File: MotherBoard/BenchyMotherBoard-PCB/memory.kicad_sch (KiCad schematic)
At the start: 2 parts

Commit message: Add MORE regulators, USB, Display, and SDCard
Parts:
- removed U?: AS4C64M16D3B, Daxxn_Packages:BGA96_9.0x13.0mm_P0.8mm, symbol Daxxn_IC:AS4C64M16D3B
- added C? (x2): 22uF, Capacitor_SMD:C_1210_3225Metric, symbol Device:C_Small
- added C? (x27): 100nF, Capacitor_SMD:C_0603_1608Metric, symbol Device:C_Small
- added R? (x24): 56, Resistor_SMD:R_0402_1005Metric, symbol Device:R_Small_US
- added R? (x2): 10K, Resistor_SMD:R_0402_1005Metric, symbol Device:R_Small_US
- added R? (x2): 240 1%, Resistor_SMD:R_0402_1005Metric, symbol Device:R_Small_US
- added R?: 100, Resistor_SMD:R_0402_1005Metric, symbol Device:R_Small_US
- added U?: IS43TR16256B-125KBLI, Package_BGA:BGA-96_9.0x13.0mm_Layout2x3x16_P0.8mm, symbol Daxxn_IC:IS43TR16256B-125KBLI
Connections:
- net GND: now also C?.2, C?.2, C?.2, C?.2, C?.2, C?.2, C?.2, C?.2, C?.2, C?.2, C?.2, C?.2, C?.2, C?.2, C?.2, C?.2, C?.2, C?.2, C?.2, C?.2, C?.2, C?.2, C?.2, C?.2, C?.2, C?.2, C?.2, C?.2, C?.2, R?.1, R?.1, R?.2, R?.2, U?.A9 (GND), U?.B1 (GNDQ), U?.B3 (GND), U?.B9 (GNDQ), U?.D1 (GNDQ), U?.D8 (GNDQ), U?.E1 (GND), U?.E2 (GNDQ), U?.E8 (GNDQ), U?.F9 (GNDQ), U?.G1 (GNDQ), U?.G8 (GND), U?.G9 (GNDQ), U?.J2 (GND), U?.J8 (GND), U?.M1 (GND), U?.M9 (GND), U?.N1 (GND), U?.P1 (GND), U?.P9 (GND), U?.T1 (GND), U?.T9 (GND)
- net VDD: now also C?.1, C?.1, C?.1, C?.1, C?.1, C?.1, C?.1, C?.1, C?.1, C?.1, C?.1, C?.1, U?.A1 (VDDQ), U?.A8 (VDDQ), U?.B2 (VDD), U?.C1 (VDDQ), U?.C9 (VDDQ), U?.D2 (VDDQ), U?.D9 (VDD), U?.E9 (VDDQ), U?.F1 (VDDQ), U?.G7 (VDD), U?.H2 (VDDQ), U?.H9 (VDDQ), U?.K2 (VDD), U?.K8 (VDD), U?.N9 (VDD), U?.R1 (VDD), U?.R9 (VDD)
- net DDR-DQ0: now reaches U?.A17 (DDR-DQ0)
- net DDR-DQ0: now also U?.D7 (DQU0)
- net DDR-DQ1: now reaches U?.A18 (DDR-DQ1)
- net DDR-DQ1: now also U?.C3 (DQU1)
- net DDR-DQ3: now reaches U?.B17 (DDR-DQ3)
- net DDR-DQ3: now also U?.C2 (DQU3)
- net DDR-DQ7: now reaches U?.B18 (DDR-DQ7)
- net DDR-DQ7: now also U?.A3 (DQU7)
- net DDR-DQSL-: now reaches U?.B19 (DDR-DQS0N)
- net DDR-DQSL-: now also U?.G3 (DQSL-)
- net DDR-DQML: now reaches U?.C18 (DDR-DQM0)
- net DDR-DQML: now also U?.E7 (DML)
- net DDR-DQSL+: now reaches U?.C19 (DDR-DQS0P)
- net DDR-DQSL+: now also U?.F3 (DQSL+)
- net DDR-DQ5: now reaches U?.D17 (DDR-DQ5)
- net DDR-DQ5: now also U?.A2 (DQU5)
- net DDR-DQ2: now reaches U?.D18 (DDR-DQ2)
- net DDR-DQ2: now also U?.C8 (DQU2)
- net DDR-DQ6: now reaches U?.D19 (DDR-DQ6)
- net DDR-DQ6: now also U?.B8 (DQU6)
- net DDR-A7: now reaches U?.E17 (DDR-A7)
- net DDR-A7: now also R?.1, U?.R2 (A7)
- net DDR-DQ4: now reaches U?.E18 (DDR-DQ4)
- net DDR-DQ4: now also U?.A7 (DQU4)
- net DDR-A13: now reaches U?.F17 (DDR-A13)
- net DDR-A13: now also R?.1, U?.T3 (A13)
- net at U?.F18 (DDR-ZQ): now also R?.1
- net DDR-A3: now reaches U?.F19 (DDR-A3)
- net DDR-A3: now also R?.1, U?.N2 (A3)
- net DDR-RESET: now reaches U?.G16 (DDR-RESET)
- net DDR-RESET: now also R?.2, U?.T2 (~{RESET})
- net DDR-A9: now reaches U?.G17 (DDR-A9)
- net DDR-A9: now also R?.1, U?.R3 (A9)
- net DDR-A2: now reaches U?.G18 (DDR-A2)
- net DDR-A2: now also R?.1, U?.P3 (A2)
- net DDR-BA0: now reaches U?.G19 (DDR-BA0)
- net DDR-BA0: now also R?.1, U?.M2 (BA0)
- net DDR-A5: now reaches U?.H17 (DDR-A5)
- net DDR-A5: now also R?.1, U?.P2 (A5)
- net DDR-A0: now reaches U?.H18 (DDR-A0)
- net DDR-A0: now also R?.1, U?.N3 (A0)
- net DDR-ODT: now reaches U?.H19 (DDR-ODT)
- net DDR-ODT: now also R?.1, U?.K1 (ODT)
- net DDR-BA2: now reaches U?.J16 (DDR-BA2)
- net DDR-BA2: now also R?.1, U?.M3 (BA2)
- net DDR-~{WE}: now reaches U?.J17 (DDR-WEN)
- net DDR-~{WE}: now also R?.1, U?.L3 (~{WE})
- net DDR-~{CS}: now reaches U?.J18 (DDR-CSN)
- net DDR-~{CS}: now also R?.1, U?.L2 (~{CS})
- net DDR-~{CAS}: now reaches U?.K17 (DDR-CASN)
- net DDR-~{CAS}: now also R?.1, U?.K3 (~{CAS})
- net DDR-CLK-: now reaches U?.K19 (DDR-CLKN)
- net DDR-CLK-: now also R?.1, U?.K7 (CK-)
- net DDR-A12: now reaches U?.L17 (DDR-A12)
- net DDR-A12: now also R?.1, U?.N7 (A12/~{BC})
- net DDR-~{RAS}: now reaches U?.L18 (DDR-RASN)
- net DDR-~{RAS}: now also R?.1, U?.J3 (~{RAS})
- net DDR-CLK+: now reaches U?.L19 (DDR-CLKP)
- net DDR-CLK+: now also R?.2, U?.J7 (CK+)
- net DDR-A1: now reaches U?.M17 (DDR-A1)
- net DDR-A1: now also R?.1, U?.P7 (A1)
- net DDR-A11: now reaches U?.M18 (DDR-A11)
- net DDR-A11: now also R?.1, U?.R7 (A11)
- net DDR-A10: now reaches U?.M19 (DDR-A10)
- net DDR-A10: now also R?.1, U?.L7 (A10/AP)
- net DDR-A6: now reaches U?.N16 (DDR-A6)
- net DDR-A6: now also R?.1, U?.R8 (A6)
- net DDR-BA1: now reaches U?.N17 (DDR-BA1)
- net DDR-BA1: now also R?.1, U?.N8 (BA1)
- net DDR-A14: now reaches U?.N18 (DDR-A14)
- net DDR-A14: now also R?.1, U?.T7 (A14)
- net DDR-A4: now reaches U?.P17 (DDR-A4)
- net DDR-A4: now also R?.1, U?.P8 (A4)
- net DDR-DQ8: now reaches U?.P18 (DDR-DQ8)
- net DDR-DQ8: now also U?.E3 (DQL0)
- net DDR-CKE: now reaches U?.P19 (DDR-CKE)
- net DDR-CKE: now also R?.1, R?.2, U?.K9 (CKE)
- net DDR-A8: now reaches U?.R17 (DDR-A8)
- net DDR-A8: now also R?.1, U?.T8 (A8)
- net DDR-DQ10: now reaches U?.R18 (DDR-DQ10)
- net DDR-DQ10: now also U?.F2 (DQL2)
- net DDR-DQ9: now reaches U?.T17 (DDR-DQ9)
- net DDR-DQ9: now also U?.F7 (DQL1)
- net DDR-DQ13: now reaches U?.T18 (DDR-DQ13)
- net DDR-DQ13: now also U?.H8 (DQL5)
- net DDR-DQSU-: now reaches U?.T19 (DDR-DQS1N)
- net DDR-DQSU-: now also U?.B7 (DQSU-)
- net DDR-DQMU: now reaches U?.U18 (DDR-DQM1)
- net DDR-DQMU: now also U?.D3 (DMU)
- net DDR-DQSU+: now reaches U?.U19 (DDR-DQS1P)
- net DDR-DQSU+: now also U?.C7 (DQSU+)
- net DDR-DQ14: now reaches U?.V18 (DDR-DQ14)
- net DDR-DQ14: now also U?.G2 (DQL6)
- net DDR-DQ11: now reaches U?.V19 (DDR-DQ11)
- net DDR-DQ11: now also U?.F8 (DQL3)
- net VREF-DDR: now reaches U?.W16 (DDR-VREF)
- net VREF-DDR: now also C?.1, C?.1, C?.1, U?.H1 (VREFQ), U?.M8 (VREFCA)
- net DDR-DQ15: now reaches U?.W17 (DDR-DQ15)
- net DDR-DQ15: now also U?.H7 (DQL7)
- net DDR-DQ12: now reaches U?.W18 (DDR-DQ12)
- net DDR-DQ12: now also U?.H3 (DQL4)
- new net: U?.J1 (NC), U?.J9 (NC), U?.L1 (NC), U?.L9 (NC), U?.M7 (NC)
- new net: R?.1, U?.L8 (ZQ)
- new net VTT-DDR: C?.1, C?.1, C?.1, C?.1, C?.1, C?.1, C?.1, C?.1, C?.1, C?.1, C?.1, C?.1, C?.1, C?.1, R?.2, R?.2, R?.2, R?.2, R?.2, R?.2, R?.2, R?.2, R?.2, R?.2, R?.2, R?.2, R?.2, R?.2, R?.2, R?.2, R?.2, R?.2, R?.2, R?.2, R?.2, R?.2, R?.2, R?.2
- no-connect marks 0 -> 4
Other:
- moved on the sheet: U?C

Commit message: Initial schematic lock
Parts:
- removed C?: 100nF, Capacitor_SMD:C_0603_1608Metric, symbol Device:C_Small
- added C100, C101, C102, C104, C99: 100nF, Capacitor_SMD:C_0603_1608Metric, symbol Device:C_Small
- added R41, R42, R43, R44, R45, R46: 1K, Resistor_SMD:R_0402_1005Metric, symbol Device:R_Small_US
- gave numbers to parts that had none: 59
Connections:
- net GND: now also C100.2, C101.2, C102.2, C104.2, C99.2, R42.1, R45.1, R46.1
- net VDD: now also C103.1, C105.1, C101.1, C99.1, R41.2, R43.2, R44.2
- removed net VREF-DDR: C103.1, C105.1, U11.H1 (VREFQ), U11.M8 (VREFCA), U2.W16 (DDR-VREF)
- new net: C102.1, R43.1, R45.2, U2.W16 (DDR-VREF)
- new net: C104.1, R44.1, R46.2, U11.M8 (VREFCA)
- new net: C100.1, R41.1, R42.2, U11.H1 (VREFQ)
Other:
- moved on the sheet: C103, C105, C106, C107, C108, C109, C110, C111, C112, C113, C114, C115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

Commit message: (WIP) Start layout
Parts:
- renumbered C99 to C100, C100 to C101, C101 to C102, C102 to C103, C103 to C104, C104 to C105, C105 to C106, C106 to C107, C107 to C108, C108 to C109, C109 to C110, C110 to C111, C111 to C112, C112 to C113, C113 to C114, C114 to C115, C115 to C116, C116 to C117, C117 to C118, C118 to C119, C119 to C120, C120 to C121, C121 to C122, C122 to C123, C123 to C124, C124 to C125, C125 to C126, C126 to C127, C127 to C128, C128 to C129, C129 to C130, C130 to C131, C131 to C132, U11 to U12
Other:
- title: Benchy Version 2 -> Benchy Reloaded

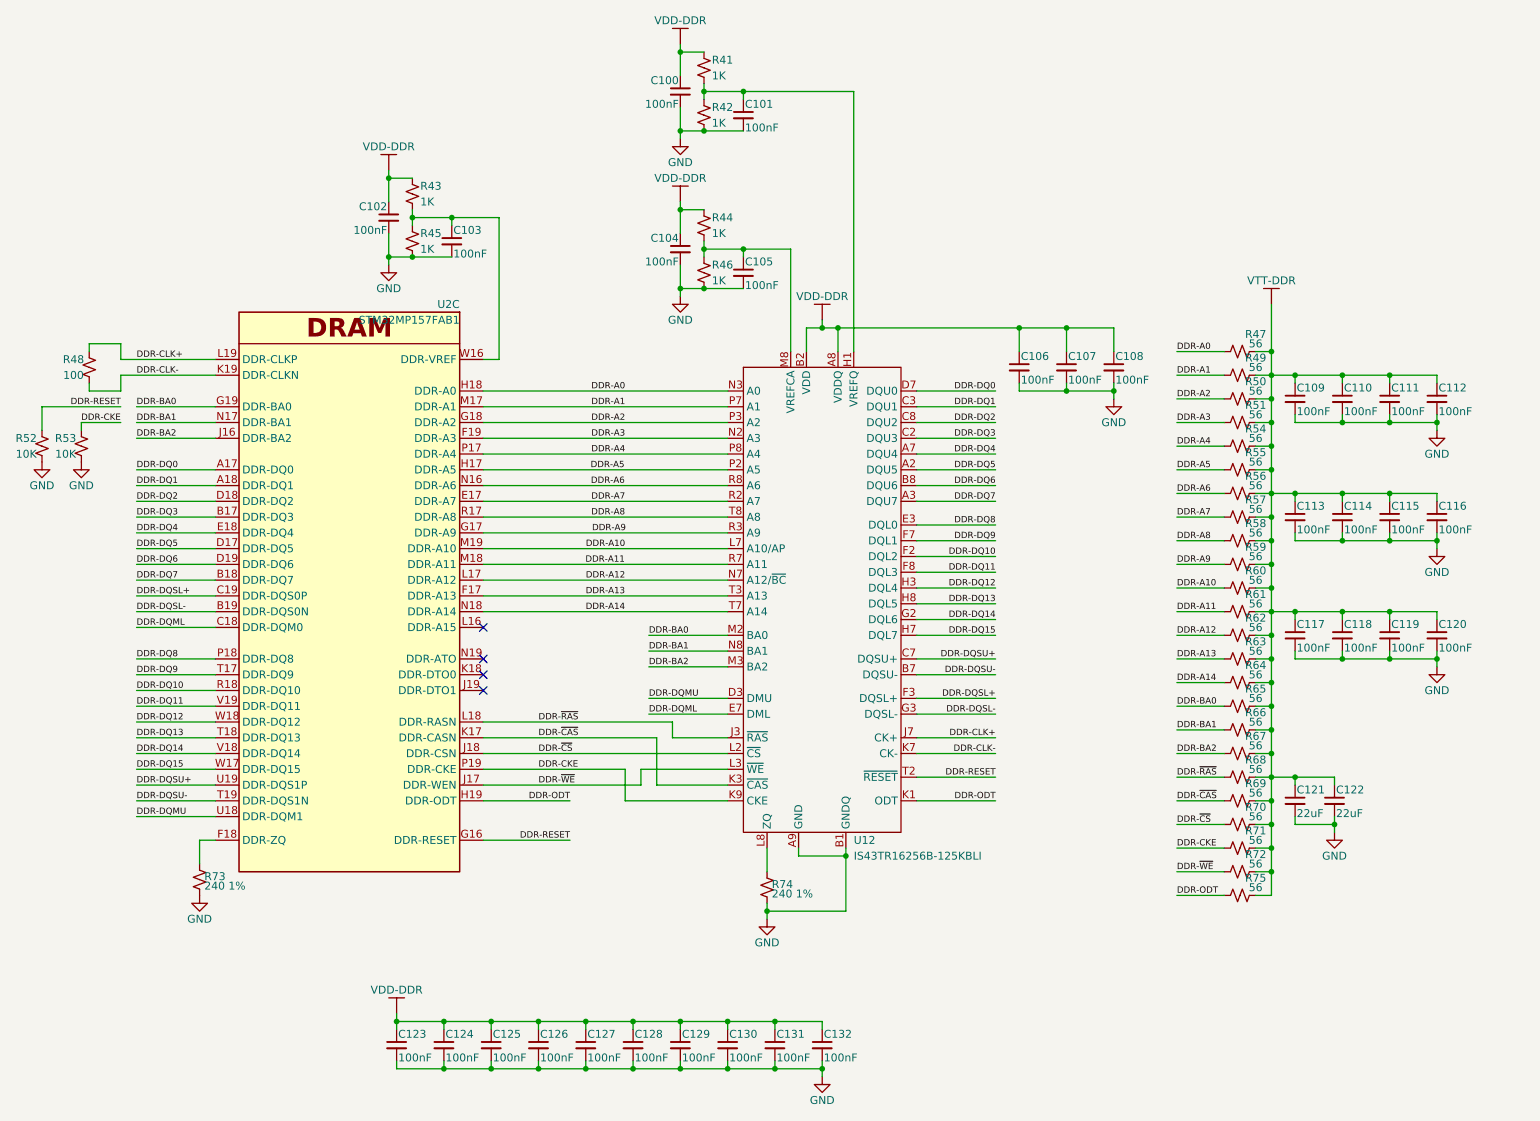
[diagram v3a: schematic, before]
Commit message: (WIP) Replaced DDR VRef with reg and started layout
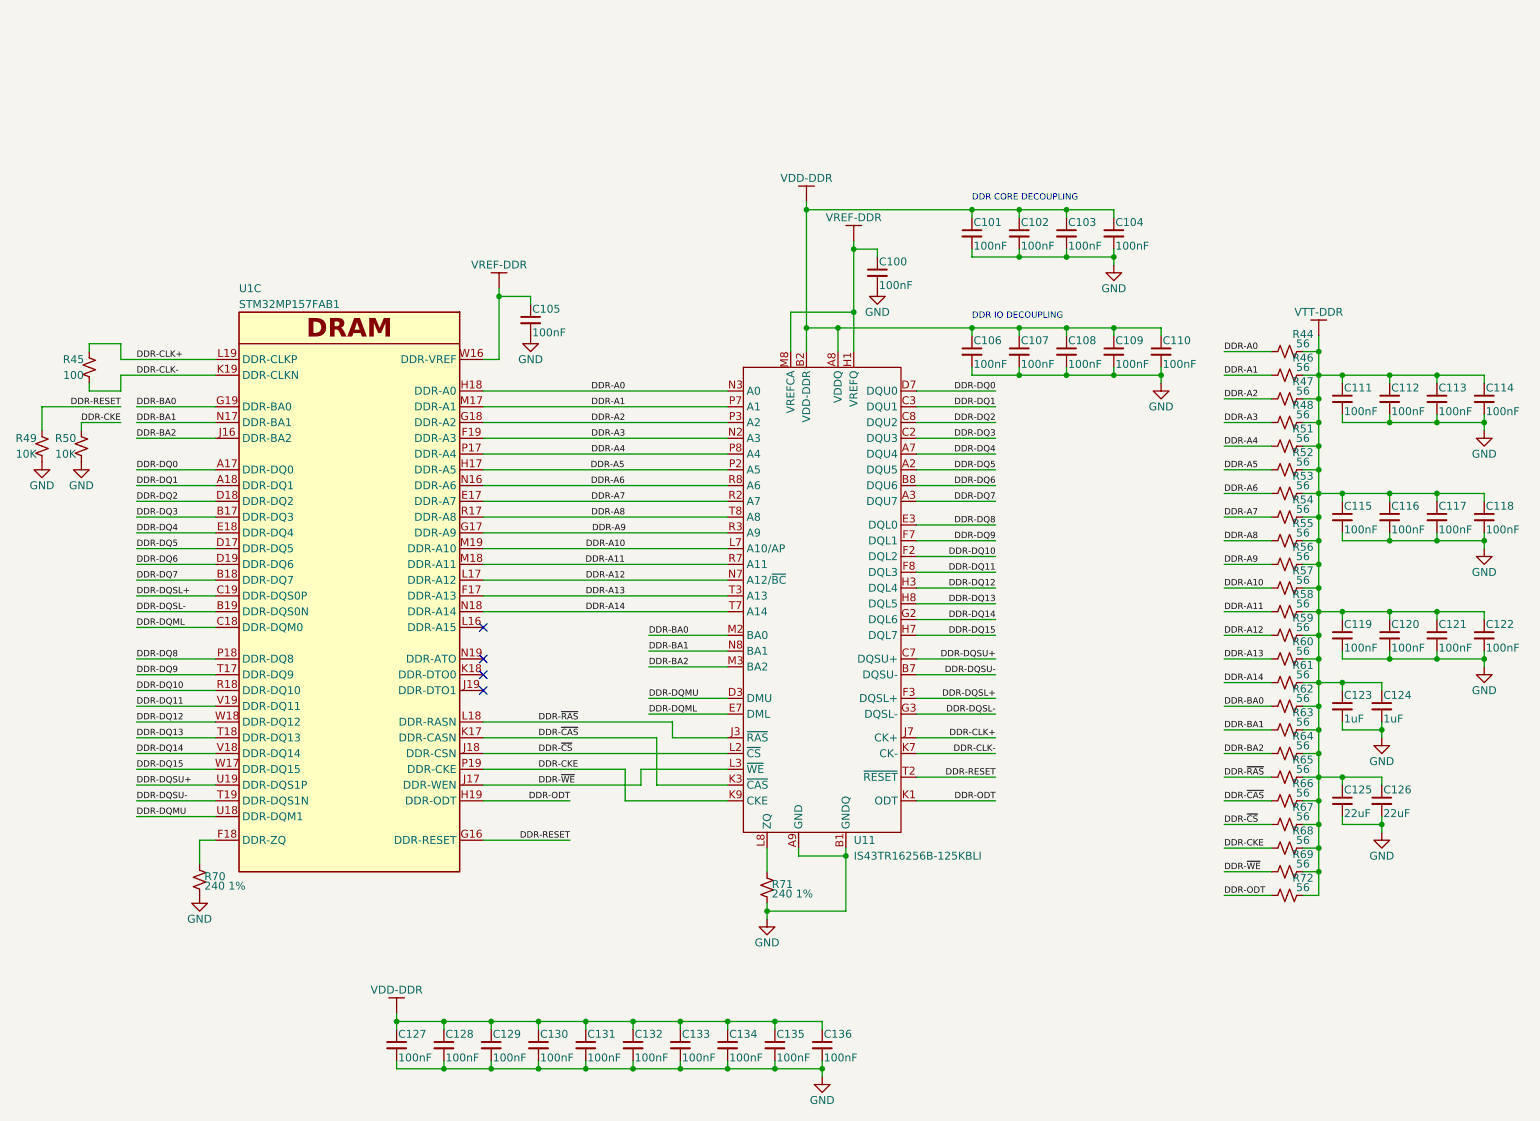
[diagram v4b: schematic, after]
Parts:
- removed R41, R42, R43, R44, R45, R46: 1K, Resistor_SMD:R_0402_1005Metric, symbol Device:R_Small_US
- added C106, C108: 100nF, Capacitor_SMD:C_0603_1608Metric, symbol Device:C_Small
- added C123, C124: 1uF, Capacitor_SMD:C_0603_1608Metric, symbol Device:C_Small
- C100, C105: footprint Capacitor_SMD:C_0603_1608Metric -> Capacitor_SMD:C_0402_1005Metric
- C111: renamed from C109; footprint Capacitor_SMD:C_0603_1608Metric -> Capacitor_SMD:C_0402_1005Metric
- C112: renamed from C110; footprint Capacitor_SMD:C_0603_1608Metric -> Capacitor_SMD:C_0402_1005Metric
- C113: renamed from C111; footprint Capacitor_SMD:C_0603_1608Metric -> Capacitor_SMD:C_0402_1005Metric
- C114: renamed from C112; footprint Capacitor_SMD:C_0603_1608Metric -> Capacitor_SMD:C_0402_1005Metric
- C115: renamed from C113; footprint Capacitor_SMD:C_0603_1608Metric -> Capacitor_SMD:C_0402_1005Metric
- C116: renamed from C114; footprint Capacitor_SMD:C_0603_1608Metric -> Capacitor_SMD:C_0402_1005Metric
- C117: renamed from C115; footprint Capacitor_SMD:C_0603_1608Metric -> Capacitor_SMD:C_0402_1005Metric
- C118: renamed from C116; footprint Capacitor_SMD:C_0603_1608Metric -> Capacitor_SMD:C_0402_1005Metric
- C119: renamed from C117; footprint Capacitor_SMD:C_0603_1608Metric -> Capacitor_SMD:C_0402_1005Metric
- C120: renamed from C118; footprint Capacitor_SMD:C_0603_1608Metric -> Capacitor_SMD:C_0402_1005Metric
- C121: renamed from C119; footprint Capacitor_SMD:C_0603_1608Metric -> Capacitor_SMD:C_0402_1005Metric
- C122: renamed from C120; footprint Capacitor_SMD:C_0603_1608Metric -> Capacitor_SMD:C_0402_1005Metric
- C127: renamed from C123; footprint Capacitor_SMD:C_0603_1608Metric -> Capacitor_SMD:C_0402_1005Metric
- C128: renamed from C124; footprint Capacitor_SMD:C_0603_1608Metric -> Capacitor_SMD:C_0402_1005Metric
- C129: renamed from C125; footprint Capacitor_SMD:C_0603_1608Metric -> Capacitor_SMD:C_0402_1005Metric
- C130: renamed from C126; footprint Capacitor_SMD:C_0603_1608Metric -> Capacitor_SMD:C_0402_1005Metric
- C131: renamed from C127; footprint Capacitor_SMD:C_0603_1608Metric -> Capacitor_SMD:C_0402_1005Metric
- C132: renamed from C128; footprint Capacitor_SMD:C_0603_1608Metric -> Capacitor_SMD:C_0402_1005Metric
- C133: renamed from C129; footprint Capacitor_SMD:C_0603_1608Metric -> Capacitor_SMD:C_0402_1005Metric
- C134: renamed from C130; footprint Capacitor_SMD:C_0603_1608Metric -> Capacitor_SMD:C_0402_1005Metric
- C135: renamed from C131; footprint Capacitor_SMD:C_0603_1608Metric -> Capacitor_SMD:C_0402_1005Metric
- C136: renamed from C132; footprint Capacitor_SMD:C_0603_1608Metric -> Capacitor_SMD:C_0402_1005Metric
- renumbered C106 to C107, C107 to C109, C108 to C110, C121 to C125, C122 to C126, R47 to R44, R48 to R45, R49 to R46, R50 to R47, R51 to R48, R52 to R49, R53 to R50, R54 to R51, R55 to R52, R56 to R53, R57 to R54, R58 to R55, R59 to R56, R60 to R57, R61 to R58, R62 to R59, R63 to R60, R64 to R61, R65 to R62, R66 to R63, R67 to R64, R68 to R65, R69 to R66, R70 to R67, R71 to R68, R72 to R69, R73 to R70, R74 to R71, R75 to R72, U2 to U1, U12 to U11
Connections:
- net GND: now also C106.2, C108.2, C123.2, C124.2
- net VTT-DDR: now also C123.1, C124.1
- net VDD-DDR: now reaches C103.1
- net VDD-DDR: now also C101.1, C102.1, C104.1, C107.1, C109.1, C110.1, C127.1, C128.1, C129.1, C130.1, C131.1, C132.1, C133.1, C134.1, C135.1, C136.1, U11.A1 (VDDQ), U11.A8 (VDDQ), U11.B2 (VDD-DDR), U11.C1 (VDDQ), U11.C9 (VDDQ), U11.D2 (VDDQ), U11.D9 (VDD-DDR), U11.E9 (VDDQ), U11.F1 (VDDQ), U11.G7 (VDD-DDR), U11.H2 (VDDQ), U11.H9 (VDDQ), U11.K2 (VDD-DDR), U11.K8 (VDD-DDR), U11.N9 (VDD-DDR), U11.R1 (VDD-DDR), U11.R9 (VDD-DDR), C106.1, C108.1; no longer U1.W16 (DDR-VREF)
- net VREF-DDR: now reaches C105.1, U11.M8 (VREFCA)
- net VREF-DDR: now also C100.1, U1.W16 (DDR-VREF), U11.H1 (VREFQ)
- removed net VDD: C100.1, C102.1, C104.1, C107.1, C109.1, C110.1, C127.1, C128.1, C129.1, C130.1, C131.1, C132.1, C133.1, C134.1, C135.1, C136.1, U11.A1 (VDDQ), U11.A8 (VDDQ), U11.B2 (VDD), U11.C1 (VDDQ), U11.C9 (VDDQ), U11.D2 (VDDQ), U11.D9 (VDD), U11.E9 (VDDQ), U11.F1 (VDDQ), U11.G7 (VDD), U11.H2 (VDDQ), U11.H9 (VDDQ), U11.K2 (VDD), U11.K8 (VDD), U11.N9 (VDD), U11.R1 (VDD), U11.R9 (VDD)
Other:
- note added: "DDR CORE DECOUPLING"
- note added: "DDR IO DECOUPLING"
- moved on the sheet: C107, C109, C110, C111, C112, C113, C114, C115, C116, C117, C118, C119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
